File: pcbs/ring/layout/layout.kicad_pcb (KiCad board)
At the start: 2 copper layers, 62 x 6.2 mm, 60 parts, among them U1 ?, U10 ?, U11 ?, U12 ?, U13 ?, U14 ?, U15 ?, U2 ?, U3 ?, U4 ?, U5 ?, U6 ?, U7 ?, U8 ?, U9 ?, Y1 32MHz

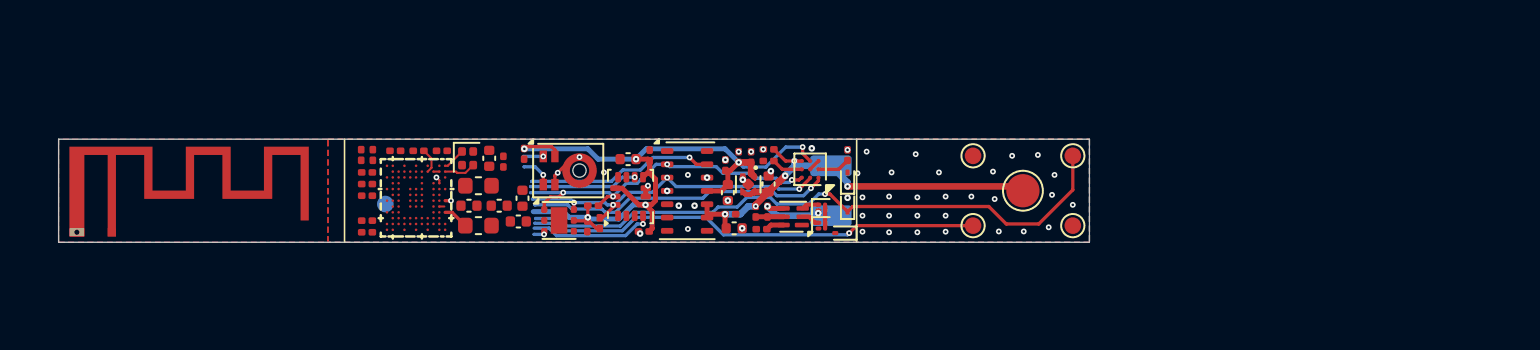
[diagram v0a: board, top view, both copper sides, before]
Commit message: layout and custom footprint for clearance
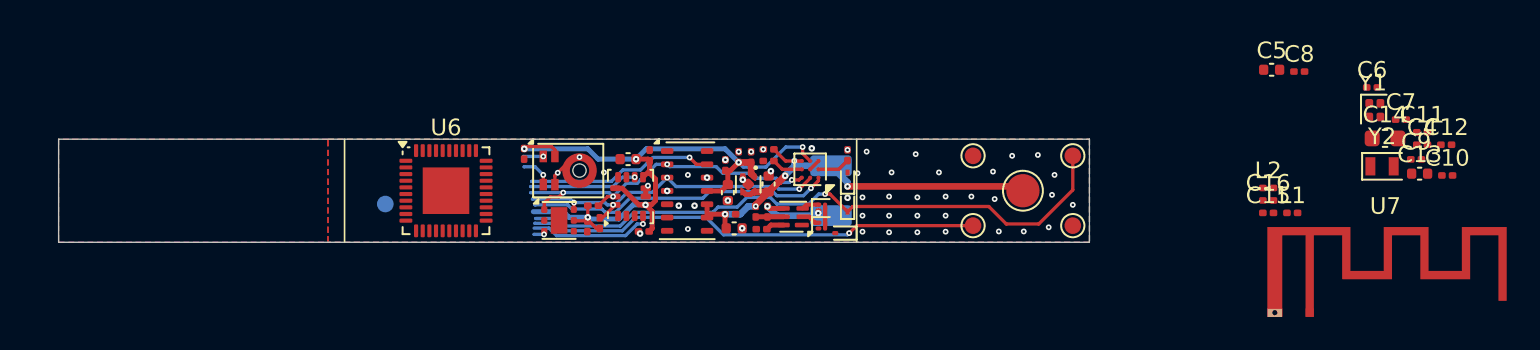
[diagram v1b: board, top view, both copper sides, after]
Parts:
- removed the C17 at (138.0, 81.0)
- removed L3, L4: 2.2nH, L_0201_0603Metric:L_0201_0603Metric
- added Y2: 32.768kHz, Crystal_SMD_2012-2Pin_2.0x1.2mm:Crystal_SMD_2012-2Pin_2.0x1.2mm, F.Cu at (199.4, 81.6)
- C10, C4, C8, C9: value 100nF -> 12pF
- C11: value 1uF -> 100nF; footprint C_0402_1005Metric:C_0402_1005Metric -> C_0201_0603Metric:C_0201_0603Metric
- C12: value 1uF -> 100pF; footprint C_0402_1005Metric:C_0402_1005Metric -> C_0201_0603Metric:C_0201_0603Metric
- C14: value 1uF -> 4.7uF; footprint C_0402_1005Metric:C_0402_1005Metric -> C_0603_1608Metric:C_0603_1608Metric
- C15: value 1uF -> 1pF; footprint C_0402_1005Metric:C_0402_1005Metric -> C_0201_0603Metric:C_0201_0603Metric
- C16: value 2.2nF -> 1.2pF
- C5: value 100nF -> 1uF; footprint C_0201_0603Metric:C_0201_0603Metric -> C_0402_1005Metric:C_0402_1005Metric
- L1: value 10uH -> 4.7nH; footprint L_0603_1608Metric:L_0603_1608Metric -> L_0201_0603Metric:L_0201_0603Metric
- L2: value 10uH -> 2.2nH; footprint L_0603_1608Metric:L_0603_1608Metric -> L_0201_0603Metric:L_0201_0603Metric
- U6: footprint WLCSP95_4.390X3.994_NOR:WLCSP95_4.390X3.994_NOR -> Modified_QFN-40_5.0mmx5.0mm:Modified_QFN-40_5.0mmx5.0mm
- Y1: footprint Crystal_SMD_2016-4Pin_2.0x1.6mm:Crystal_SMD_2016-4Pin_2.0x1.6mm -> Crystal_SMD_1210-4Pin_1.2x1.0mm:Crystal_SMD_1210-4Pin_1.2x1.0mm
- moved U7 72.2 mm to (195.1, 90.4)
- moved C10 63.3 mm to (203.3, 82.2), turned to 0 degrees
- moved C9 63.2 mm to (201.4, 81.2), turned to 0 degrees
- moved C7 62.4 mm to (200.5, 78.8), turned to 0 degrees
- moved C6 61.1 mm to (198.8, 76.9), turned to 0 degrees
- moved C4 59.0 mm to (201.8, 80.3), turned to 0 degrees
- moved C12 58.9 mm to (203.3, 80.3)
- moved C8 56.5 mm to (194.4, 75.9), turned to 0 degrees
- moved C11 55.7 mm to (201.8, 79.6)
- moved Y1 54.6 mm to (199.0, 78.3)
- moved C13 54.0 mm to (201.7, 82.1), turned to 0 degrees
- moved C14 52.4 mm to (199.6, 80.0)
- moved C5 51.5 mm to (192.8, 75.8), turned to 0 degrees
- moved L1 49.0 mm to (194.0, 84.4)
- moved L2 47.5 mm to (192.6, 82.9)
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- renumbered C18 to C17, C19 to C18, C20 to C19, C21 to C20, C22 to C21, C23 to C22, C24 to C23, C25 to C24, C26 to C25, C27 to C26, C28 to C27, C29 to C28
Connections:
- C10 pad 1: cpu.decn -> cpu.xl2
- C11 pad 1: cpu.deca -> cpu.dec1
- C12 pad 1: VDD -> cpu.dec3
- C13 pad 1: VDD -> cpu.dec4_6
- C14 pad 1: cpu.decd -> VDD
- C15 pad 1: cpu.decr -> cpu.ant_match.n1
- C16 pad 1: cpu.decr -> cpu.ant_match.n2
- C4 pad 1: VDD -> cpu.xin
- C8 pad 1: VDD -> cpu.xout
- C9 pad 1: VDD -> cpu.xl1
- L1 pad 1: cpu.dccd -> cpu.ant
- L1 pad 2: cpu.decd -> cpu.ant_match.n1
- L2 pad 1: cpu.dcc -> cpu.ant_match.n1
- L2 pad 2: cpu.decr -> cpu.ant_match.n2
- U7 pad 1: cpu.antenna.n2 -> cpu.ant_match.ANT_OUT
- Y1 pad 1: cpu.xc1 -> cpu.xin
- Y1 pad 3: cpu.xc2 -> cpu.xout
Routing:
- net cpu.xc2: track 1.91 -> 0.00 mm
- net VDD: track 47.8 -> 46.2 mm
- net cpu.dccd: track 1.54 -> 0.00 mm
- net cpu.xc1: track 1.37 -> 0.00 mm
- net cpu.decr: track 0.42 -> 0.00 mm, vias 1 -> 0
- net cpu.decd: track 0.35 -> 0.00 mm, vias 1 -> 0

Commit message: routed
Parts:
- added C17: 1.2pF, C_0201_0603Metric:C_0201_0603Metric, F.Cu at (136.3, 81.6)
- added L3: 4.7nH, L_0201_0603Metric:L_0201_0603Metric, F.Cu at (137.3, 82.0)
- added L4: 2.2nH, L_0201_0603Metric:L_0201_0603Metric, F.Cu at (136.3, 80.5)
- C11: value 100nF -> 12pF
- C12: value 100pF -> 100nF
- C13: value 1uF -> 100pF; footprint C_0402_1005Metric:C_0402_1005Metric -> C_0201_0603Metric:C_0201_0603Metric
- C14: value 4.7uF -> 1uF; footprint C_0603_1608Metric:C_0603_1608Metric -> C_0402_1005Metric:C_0402_1005Metric
- C15: value 1pF -> 47nF
- C16: value 1.2pF -> 1pF
- C5: value 1uF -> 4.7uF; footprint C_0402_1005Metric:C_0402_1005Metric -> C_0603_1608Metric:C_0603_1608Metric
- C6: value 100nF -> 1uF; footprint C_0201_0603Metric:C_0201_0603Metric -> C_0402_1005Metric:C_0402_1005Metric
- C8: value 12pF -> 100nF
- L1: value 4.7nH -> 10uH; footprint L_0201_0603Metric:L_0201_0603Metric -> L_0603_1608Metric:L_0603_1608Metric
- L2: value 2.2nH -> 15nH; footprint L_0201_0603Metric:L_0201_0603Metric -> L_0402_1005Metric:L_0402_1005Metric
- U7: footprint Texas_SWRA117D_2.4GHz_Right:Texas_SWRA117D_2.4GHz_Right -> Texas_SWRA117D_2.4GHz_Left:Texas_SWRA117D_2.4GHz_Left
- Y2: footprint Crystal_SMD_2012-2Pin_2.0x1.2mm:Crystal_SMD_2012-2Pin_2.0x1.2mm -> Crystal_SMD_1210-4Pin_1.2x1.0mm:Crystal_SMD_1210-4Pin_1.2x1.0mm
- moved U7 74.2 mm to (121.5, 80.6), turned to 180 degrees
- moved C4 66.0 mm to (135.8, 83.0), turned to 90 degrees
- moved C13 65.9 mm to (135.8, 84.5), turned to -90 degrees
- moved C9 65.3 mm to (136.3, 85.7), turned to 180 degrees
- moved C7 63.2 mm to (137.7, 85.7), turned to 180 degrees
- moved C14 62.5 mm to (137.1, 82.8), turned to 180 degrees
- moved Y1 62.3 mm to (137.0, 84.4)
- moved C12 58.9 mm to (144.6, 85.7)
- moved C10 57.4 mm to (146.0, 85.7), turned to 180 degrees
- moved C8 56.9 mm to (137.7, 80.5), turned to 180 degrees
- moved C11 55.3 mm to (146.7, 83.6)
- moved C16 55.3 mm to (137.3, 81.2)
- moved Y2 54.4 mm to (145.1, 84.2), turned to 180 degrees
- moved C6 52.5 mm to (146.9, 84.8), turned to 180 degrees
- moved L1 48.3 mm to (145.8, 82.5)
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- renumbered C17 to C18, C18 to C19, C19 to C20, C20 to C21, C21 to C22, C22 to C23, C23 to C24, C24 to C25, C25 to C26, C26 to C27, C27 to C28, C28 to C29
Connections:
- net cpu.NC_14 renamed NC
- net cpu.NC_15 renamed NC_2
- net cpu.NC_16 renamed NC_3
- net cpu.NC_17 renamed NC_4
- net cpu.NC_8 renamed nfc1
- net cpu.NC_9 renamed nfc2
- C10 pad 1: cpu.xl2 -> cpu.xl1
- C11 pad 1: cpu.dec1 -> cpu.xl2
- C12 pad 1: cpu.dec3 -> cpu.dec1
- C13 pad 1: cpu.dec4_6 -> cpu.dec3
- C14 pad 1: VDD -> cpu.dec4_6
- C15 pad 1: cpu.ant_match.n1 -> cpu.dec4_6
- C16 pad 1: cpu.ant_match.n2 -> cpu.antenna.n1
- C8 pad 1: cpu.xout -> VDD
- C9 pad 1: cpu.xl1 -> cpu.xout
- L1 pad 1: cpu.ant -> cpu.dcc
- L1 pad 2: cpu.ant_match.n1 -> cpu.dcc_mid
- L2 pad 1: cpu.ant_match.n1 -> cpu.dcc_mid
- L2 pad 2: cpu.ant_match.n2 -> cpu.dec4_6
- U6 pad 12: cpu.NC_19 -> cpu.NC_3
- U6 pad 13: cpu.NC_20 -> cpu.NC_4
- U6 pad 14: cpu.NC_11 -> mic_data
- U6 pad 15: cpu.NC_12 -> mic_clk
- U6 pad 17: cpu.NC_13 -> hbt_int
- U6 pad 31: cpu.NC_5 -> tmp_int
- U6 pad 32: cpu.NC_4 -> imu_int1
- U6 pad 39: cpu.NC_3 -> cpu.dcc
- U6 pad 4: cpu.NC_6 -> sda
- U6 pad 5: cpu.NC_7 -> scl
- U6 pad 6: cpu.NC_18 -> bat_low
- U6 pad 7: cpu.NC_10 -> imu_int2
- U7 pad 1: cpu.ant_match.ANT_OUT -> cpu.antenna.n2
- Y2 pad 2: cpu.xl2 -> GND
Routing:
- net VDD: track 46.2 -> 81.9 mm, vias 6 -> 13
- net GND: track 4.06 -> 34.1 mm, vias 50 -> 63
- net cpu.dec4_6: track 0.00 -> 16.1 mm, vias 0 -> 5
- net cpu.antenna.n2: track 0.00 -> 15.4 mm
- net swdio: track 27.5 -> 41.4 mm, vias 1 -> 2
- net swdclk: track 37.5 -> 49.8 mm, vias 1 -> 2
- net tmp_int: track 0.60 -> 12.1 mm, vias 1 -> 2
- net imu_int1: track 7.51 -> 18.7 mm, vias 1 -> 2
- net mic_data: track 1.20 -> 11.8 mm, vias 1 -> 2
- net mic_clk: track 1.94 -> 12.1 mm, vias 1 -> 2
- net hbt_int: track 11.3 -> 21.1 mm, vias 1 -> 2
- net bat_low: track 18.4 -> 26.5 mm, vias 1 -> 2
- net sda: track 19.7 -> 27.4 mm, vias 4 -> 5
- net imu_int2: track 6.48 -> 14.0 mm, vias 1 -> 2
- net scl: track 20.7 -> 27.0 mm, vias 4 -> 5
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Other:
- board size 62 x 6.2 mm -> 63.5 x 6.2 mm

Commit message: all mpns
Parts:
- D1: renamed from U11; value ? -> ESD9B5.0ST5G
- D2: renamed from U12; value ? -> ESD9B5.0ST5G
- D3: renamed from U13; value ? -> ESD9B5.0ST5G
- U10: value ? -> IM72D128V01
- renumbered U14 to U11, U15 to U12

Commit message: all mpns
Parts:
- Q1: renamed from U3; value ? -> CSD13380F3T
- Q2: renamed from U4; value ? -> CSD13380F3T
- U1: value ? -> BQ27427YZFR
- U2: renamed from U5; value ? -> BQ29700
- U3: renamed from U6; value ? -> nRF52833-QDAA
- U4: renamed from U8; value ? -> MAX30102EFD+T
- U5: renamed from U9; value ? -> LSM6DSOX
- U6: renamed from U11; value ? -> TMP117AIDRVR
- U7: renamed from U12; value ? -> TPS7A2018PDQN
- renumbered U2 to BT1, U7 to J1, U10 to MK1
